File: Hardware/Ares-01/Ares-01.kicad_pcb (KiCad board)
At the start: 2 copper layers, 31 parts, among them J1 BTS7960_1, J12 XT60, J13 TCRT5000_1, J14 TCRT5000_2, J15 TCRT5000_3, J2 BTS7960_2, J3 Sharp, J4 Sharp, J5 Sharp, J6 Sharp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

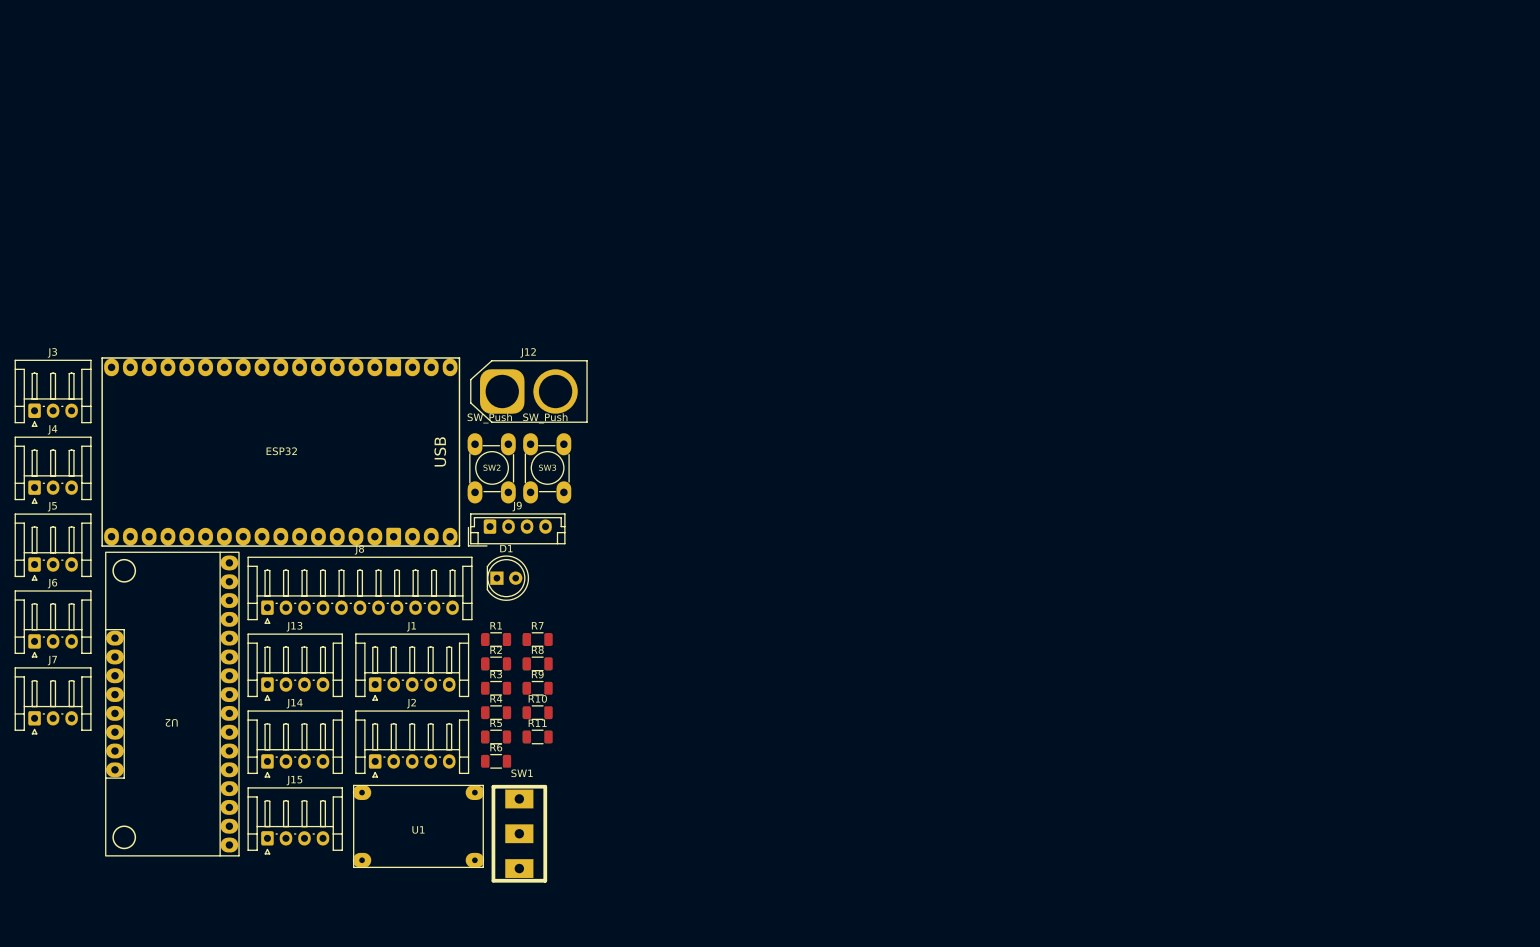
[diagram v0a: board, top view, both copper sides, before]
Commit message: Actualizacion de huellas
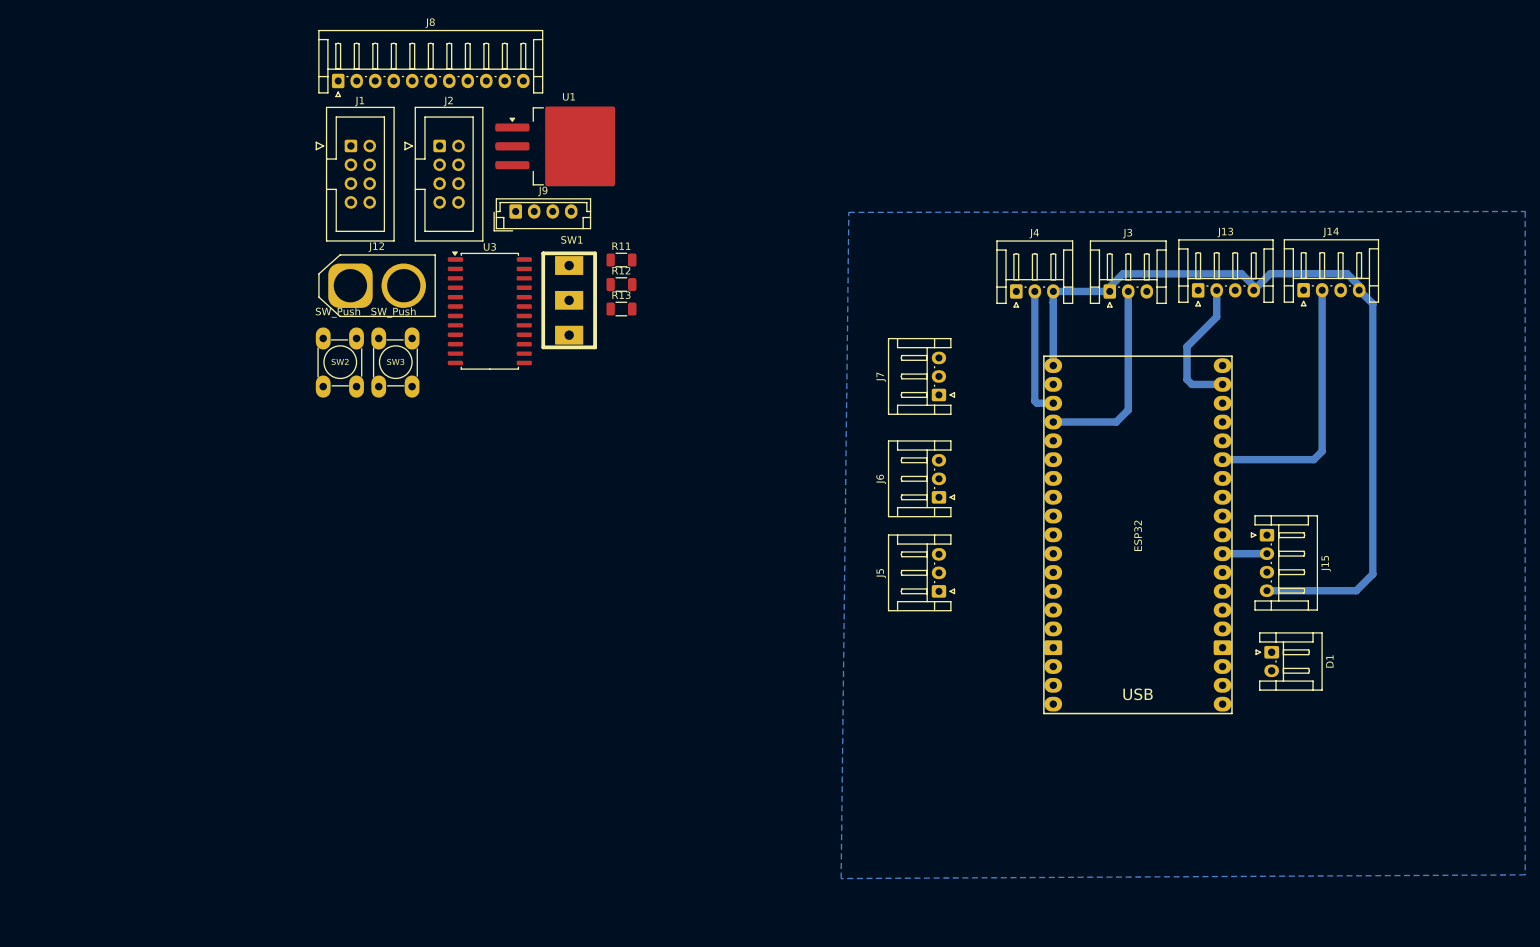
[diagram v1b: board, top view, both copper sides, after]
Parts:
- removed R1, R3, R5, R7, R9: 10k, Resistor_SMD:R_1206_3216Metric
- removed R10, R2, R4, R6, R8: 20k, Resistor_SMD:R_1206_3216Metric
- removed U2: CD74HC4067M, RamLib:CD74HC4067_module
- added R12: 220, Resistor_SMD:R_1206_3216Metric, F.Cu at (112.8, 28.4)
- added R13: 220, Resistor_SMD:R_1206_3216Metric, F.Cu at (112.8, 31.8)
- added U3: CD74HC4067M, Package_SO:SOIC-24W_7.5x15.4mm_P1.27mm, F.Cu at (95.1, 32.0)
- D1: footprint LED_THT:LED_D5.0mm -> Connector_JST:JST_EH_S2B-EH_1x02_P2.50mm_Horizontal
- ESP32: footprint RamLib:Nodemcu_ESP32S_38pin -> RamLib 2:Nodemcu_ESP32S_38pin
- J1, J2: footprint Connector_JST:JST_EH_S5B-EH_1x05_P2.50mm_Horizontal -> Connector_IDC:IDC-Header_2x04_P2.54mm_Vertical
- J9: value Conn_01x04_Pin -> Ssd1306 Arduino Pic
- SW1: footprint RamLib:SW_SPDT_TH_Vertical -> EESTN5 2:SW_SPDT_TH_Vertical
- SW2, SW3: footprint RamLib:PUSH_SWITCH_THT -> EESTN5 2:PUSH_SWITCH_THT
- U1: value Mini360 -> L7805; footprint Mini360_step-down:Mini360_step-down -> Package_TO_SOT_SMD:TO-263-3_TabPin2
- moved J14 153.7 mm to (205.0, 29.2)
- moved J3 146.1 mm to (178.8, 29.4)
- moved J15 141.1 mm to (200.0, 62.3), turned to -90 degrees
- moved J13 136.5 mm to (190.7, 29.2)
- moved J4 135.2 mm to (166.2, 29.4)
- moved J7 129.7 mm to (155.7, 43.4), turned to 90 degrees
- moved J6 123.7 mm to (155.7, 57.2), turned to 90 degrees
- moved J5 122.2 mm to (155.7, 69.9), turned to 90 degrees
- moved ESP32 116.3 mm to (182.6, 62.2), turned to -90 degrees
- moved D1 105.1 mm to (200.7, 78.1), turned to -90 degrees
- moved U1 94.1 mm to (105.8, 9.78)
- moved J2 83.6 mm to (88.3, 9.73)
- moved J1 72.8 mm to (76.3, 9.73)
- moved SW1 72.3 mm to (105.8, 30.6)
- moved J8 71.8 mm to (74.6, 0.95)
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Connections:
- D1 pad 1: LED -> Net-(D1-K)
- D1 pad 2: Net-(D1-A) -> LED
- ESP32 pad 14: unconnected-(ESP32-GND-Pad14) -> GND
- ESP32 pad 29: OUT_B -> S2
- ESP32 pad 3: OUT1 -> OUT2
- ESP32 pad 32: unconnected-(ESP32-GND-Pad32) -> GND
- ESP32 pad 33: S2 -> OUT_B
- ESP32 pad 38: unconnected-(ESP32-GND-Pad38) -> GND
- ESP32 pad 4: OUT2 -> OUT1
- ESP32 pad 6: OUT4 -> OUT5
- ESP32 pad 7: OUT5 -> OUT4
- J3 pad 1: VCC -> 3.3V
- J3 pad 2: Net-(J3-Pin_2) -> OUT1
- J4 pad 1: VCC -> GND
- J4 pad 2: Net-(J4-Pin_2) -> OUT2
- J4 pad 3: GND -> 3.3V
- J5 pad 1: VCC -> GND
- J5 pad 2: Net-(J5-Pin_2) -> OUT3
- J5 pad 3: GND -> 3.3V
- J6 pad 1: VCC -> 3.3V
- J6 pad 2: Net-(J6-Pin_2) -> OUT4
- J7 pad 1: VCC -> GND
- J7 pad 2: Net-(J7-Pin_2) -> OUT5
- J7 pad 3: GND -> 3.3V
- R11 pad 2: Net-(D1-A) -> Net-(D1-K)
- SW2 pad 2: GND -> Net-(R12-Pad2)
- SW3 pad 2: GND -> Net-(R13-Pad2)
- U1 pad 1: GND -> Net-(SW1-A)
- U1 pad 2: Net-(SW1-A) -> GND
- U1 pad 3: GND -> VCC
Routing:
- net 3.3V: track 0.00 -> 110.5 mm
- net OUT_B: track 0.00 -> 35.7 mm
- net OUT1: track 0.00 -> 26.8 mm
- net OUT_A: track 0.00 -> 18.8 mm
- net OUT2: track 0.00 -> 17.4 mm
- net OUT_C: track 0.00 -> 6.00 mm
- added copper zone on B.Cu, net GND

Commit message: primer version del pcb
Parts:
- added C2: 0,1 µF, Capacitor_SMD:C_1206_3216Metric_Pad1.33x1.80mm_HandSolder, B.Cu at (204.3, 103.8)
- added C3: 0,1uf, Capacitor_SMD:C_1206_3216Metric_Pad1.33x1.80mm_HandSolder, B.Cu at (205.0, 110.4)
- D1: footprint Connector_JST:JST_EH_S2B-EH_1x02_P2.50mm_Horizontal -> Connector_JST:JST_EH_B2B-EH-A_1x02_P2.50mm_Vertical
- J1: value BTS7960_1 -> BTS7960
- J13, J14, J15: footprint Connector_JST:JST_EH_S4B-EH_1x04_P2.50mm_Horizontal -> Connector_JST:JST_EH_B4B-EH-A_1x04_P2.50mm_Vertical
- J2: value BTS7960_2 -> BTS7960
- J3, J4, J5, J6, J7: footprint Connector_JST:JST_EH_S3B-EH_1x03_P2.50mm_Horizontal -> Connector_JST:JST_EH_B3B-EH-A_1x03_P2.50mm_Vertical
- J8: footprint Connector_JST:JST_EH_S11B-EH_1x11_P2.50mm_Horizontal -> Connector_JST:JST_EH_B10B-EH-A_1x10_P2.50mm_Vertical
- R11, R12, R13, U1: moved to B.Cu
- SW1: footprint EESTN5 2:SW_SPDT_TH_Vertical -> EESTN5:SW_SPDT_TH_Vertical
- SW2, SW3: footprint EESTN5 2:PUSH_SWITCH_THT -> EESTN5:PUSH_SWITCH_THT
- U3: footprint Package_SO:SOIC-24W_7.5x15.4mm_P1.27mm -> RamLib:CD74HC4067_module; moved to B.Cu
- moved J8 173.8 mm to (222.9, 91.4), turned to 90 degrees
- moved J1 152.5 mm to (204.0, 93.1), turned to -90 degrees
- moved U1 148.4 mm to (218.4, 106.3)
- moved J2 125.2 mm to (181.7, 93.1), turned to -90 degrees
- moved U3 119.9 mm to (209.7, 67.3), turned to 180 degrees
- moved J12 110.8 mm to (151.9, 109.6), turned to 90 degrees
- moved SW3 89.9 mm to (160.9, 75.0)
- moved J9 89.5 mm to (186.5, 35.5), turned to 180 degrees
- moved SW2 87.7 mm to (151.0, 75.0)
- moved SW1 78.0 mm to (151.9, 93.5), turned to -90 degrees
- moved R13 75.5 mm to (165.4, 85.9), turned to 90 degrees
- moved R12 71.6 mm to (155.5, 85.9), turned to 90 degrees
- moved R11 59.6 mm to (154.6, 67.7)
- moved D1 42.3 mm to (159.7, 67.7), turned to 0 degrees
- moved J4 33.3 mm to (162.2, 62.4), turned to 180 degrees
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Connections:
- ESP32 pad 11: EN_1 -> LED
- ESP32 pad 12: RPWM_2 -> B1
- ESP32 pad 15: EN_1 -> B2
- ESP32 pad 26: LED -> RPWM_2
- ESP32 pad 27: LPWM_2 -> COM
- ESP32 pad 28: OUT_C -> S0
- ESP32 pad 29: S2 -> S1
- ESP32 pad 3: OUT2 -> LPWM_2
- ESP32 pad 30: S0 -> S2
- ESP32 pad 31: S1 -> S3
- ESP32 pad 33: OUT_B -> SCL
- ESP32 pad 36: S3 -> SDA
- ESP32 pad 37: OUT_A -> unconnected-(ESP32-G23-Pad37)
- ESP32 pad 4: OUT1 -> OUT5
- ESP32 pad 5: OUT3 -> OUT4
- ESP32 pad 6: OUT5 -> OUT3
- ESP32 pad 7: OUT4 -> OUT1
- ESP32 pad 8: COM -> OUT2
- J1 pad 1: RPWM_1 -> VCC
- J1 pad 2: LPWM_1 -> GND
- J1 pad 3: EN_1 -> unconnected-(J1-Pin_3-Pad3)
- J1 pad 4: VCC -> unconnected-(J1-Pin_4-Pad4)
- J1 pad 5: GND -> VCC
- J1 pad 6: (no net) -> VCC
- J1 pad 7: (no net) -> RPWM_2
- J1 pad 8: (no net) -> LPWM_2
- J2 pad 1: RPWM_2 -> VCC
- J2 pad 2: LPWM_2 -> GND
- J2 pad 3: EN_2 -> unconnected-(J2-Pin_3-Pad3)
- J2 pad 4: VCC -> unconnected-(J2-Pin_4-Pad4)
- J2 pad 5: GND -> VCC
- J2 pad 6: (no net) -> VCC
- J2 pad 7: (no net) -> RPWM_1
- J2 pad 8: (no net) -> LPWM_1
- J3 pad 1: 3.3V -> OUT1
- J3 pad 2: OUT1 -> GND
- J3 pad 3: GND -> 3.3V
- J4 pad 1: GND -> OUT2
- J4 pad 2: OUT2 -> GND
- J5 pad 1: GND -> OUT3
- J5 pad 2: OUT3 -> GND
- J6 pad 1: 3.3V -> OUT4
- J6 pad 2: OUT4 -> GND
- J6 pad 3: GND -> 3.3V
- J7 pad 1: GND -> OUT5
- J7 pad 2: OUT5 -> GND
- U3 pad 21: unconnected-(U3-I10-Pad21) -> OUT_C
- U3 pad 22: B2 -> OUT_A
- U3 pad 23: B1 -> OUT_B
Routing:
- net VCC: track 0.00 -> 83.9 mm
- net LPWM_2: track 0.00 -> 70.5 mm
- net Net-(SW1-A): track 0.00 -> 68.6 mm
- net LPWM_1: track 0.00 -> 39.9 mm
- net RPWM_1: track 0.00 -> 38.6 mm
- net RPWM_2: track 0.00 -> 30.1 mm
- net 3.3V: track 110.5 -> 137.8 mm
- net SCL: track 0.00 -> 26.0 mm
- net B1: track 0.00 -> 20.0 mm
- net OUT_C: track 6.00 -> 25.6 mm
- net OUT1: track 26.8 -> 10.0 mm
- net SDA: track 0.00 -> 15.6 mm
- net OUT_A: track 18.8 -> 32.6 mm
- net OUT5: track 0.00 -> 11.1 mm
- net LED: track 0.00 -> 10.2 mm
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
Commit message: primera version del pcb,2
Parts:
- added C4: 0,1uf, Capacitor_SMD:C_1206_3216Metric_Pad1.33x1.80mm_HandSolder, B.Cu at (192.4, 105.4)
- added C5: 0,1 µF, Capacitor_SMD:C_1206_3216Metric_Pad1.33x1.80mm_HandSolder, B.Cu at (178.1, 111.8)
- added U2: AMS1117, Package_TO_SOT_SMD:SOT-223-3_TabPin2, B.Cu at (185.4, 108.6)
- moved R11 73.2 mm to (221.6, 97.2), turned to 180 degrees
- moved D1 64.0 mm to (216.5, 97.2), turned to 180 degrees
- moved C2 1.84 mm to (205.2, 102.2), turned to 90 degrees
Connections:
- ESP32 pad 10: LPWM_1 -> RPWM_1
- ESP32 pad 11: LED -> LPWM_1
- ESP32 pad 24: unconnected-(ESP32-G2/ADC12-Pad24) -> LED
- ESP32 pad 3: LPWM_2 -> unconnected-(ESP32-G36/ADC0-Pad3)
- ESP32 pad 9: RPWM_1 -> LPWM_2
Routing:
- net VCC: track 83.9 -> 108.3 mm
- net LED: track 10.2 -> 31.2 mm
- net LPWM_2: track 70.5 -> 49.7 mm
- net 3.3V: track 137.8 -> 143.6 mm
- net LPWM_1: track 39.9 -> 35.4 mm
- net RPWM_1: track 38.6 -> 34.4 mm
- net Net-(D1-K): track 3.66 -> 0.00 mm
- net RPWM_2: track 30.1 -> 30.9 mm

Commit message: Version 2.1 PCB
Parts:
- J12: footprint Connector_AMASS:AMASS_XT60-F_1x02_P7.20mm_Vertical -> RamLib2:XT30 connector
- moved C4 44.8 mm to (150.2, 90.5), turned to 90 degrees
- moved U2 32.7 mm to (155.9, 94.4), turned to 0 degrees
- moved C5 32.1 mm to (150.2, 96.0), turned to -90 degrees
- moved SW1 10.6 mm to (151.9, 104.1)
- moved J12 5.25 mm to (146.9, 111.1), turned to 0 degrees
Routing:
- net 3.3V: track 143.6 -> 190.0 mm
- net GND: track 0.00 -> 35.6 mm, vias 0 -> 2
- net Net-(SW1-A): track 68.6 -> 61.7 mm
- net Net-(D1-K): track 0.00 -> 3.66 mm
- net Net-(J12-Pin_2): track 8.90 -> 6.94 mm
- net VCC: track 108.3 -> 109.0 mm

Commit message: version 2.1 PCB
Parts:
- moved J15 1.38 mm to (216.4, 43.0)
- moved J13 1.23 mm to (210.2, 43.0)
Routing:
- net VCC: track 109.0 -> 117.4 mm
- net OUT_B: track 38.7 -> 40.7 mm
- net OUT_A: track 32.6 -> 30.5 mm

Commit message: version 3 del pcb
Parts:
- removed R12, R13: 220, Resistor_SMD:R_1206_3216Metric
- C2, C3, C4, C5: footprint Capacitor_SMD:C_1206_3216Metric_Pad1.33x1.80mm_HandSolder -> Capacitor_SMD:C_0805_2012Metric
- J12: value XT60 -> XT30
- J13, J14, J15, J9: footprint Connector_JST:JST_EH_B4B-EH-A_1x04_P2.50mm_Vertical -> Connector_JST:JST_XH_B4B-XH-A_1x04_P2.50mm_Vertical
- J3, J4, J5, J6, J7: footprint Connector_JST:JST_EH_B3B-EH-A_1x03_P2.50mm_Vertical -> Connector_JST:JST_XH_B3B-XH-A_1x03_P2.50mm_Vertical
- J8: footprint Connector_JST:JST_EH_B10B-EH-A_1x10_P2.50mm_Vertical -> Connector_JST:JST_XH_B10B-XH-A_1x10_P2.50mm_Vertical
- R11: footprint Resistor_SMD:R_1206_3216Metric -> Resistor_SMD:R_0805_2012Metric
- moved C4 59.1 mm to (209.2, 93.0)
- moved U2 59.1 mm to (214.9, 96.2)
- moved C5 59.0 mm to (209.2, 97.2)
- moved R11 19.8 mm to (202.1, 100.2), turned to 90 degrees
- moved D1 14.6 mm to (202.1, 95.0), turned to 90 degrees
- moved J1 13.5 mm to (194.6, 102.8), turned to 180 degrees
- moved SW2 11.5 mm to (162.5, 74.1), turned to -90 degrees
- moved J2 11.3 mm to (176.0, 102.8), turned to 180 degrees
- moved SW3 9.16 mm to (162.5, 84.0), turned to -90 degrees
- moved J12 8.19 mm to (153.4, 106.2)
- moved SW1 8.19 mm to (158.4, 99.2)
- moved J7 5.10 mm to (162.2, 36.8)
- moved J15 3.33 mm to (219.7, 43.0)
- moved C2 3.25 mm to (205.2, 105.5)
- moved J6 3.20 mm to (162.2, 43.8)
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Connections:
- ESP32 pad 1: 3.3V -> unconnected-(ESP32-3v3-Pad1)
- SW2 pad 2: Net-(R12-Pad2) -> GND
- SW3 pad 2: Net-(R13-Pad2) -> GND
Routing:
- net B2: track 5.72 -> 19.8 mm
- net LED: track 31.2 -> 21.6 mm
- net OUT5: track 11.1 -> 18.1 mm
- net GND: track 35.6 -> 41.0 mm
- net LPWM_2: track 49.7 -> 54.6 mm
- net RPWM_1: track 34.4 -> 38.5 mm
- net OUT_C: track 25.7 -> 29.6 mm
- net OUT_B: track 40.7 -> 37.4 mm
- net Net-(R13-Pad2): track 2.99 -> 0.00 mm
- net Net-(R12-Pad2): track 2.99 -> 0.00 mm
- net Net-(SW1-A): track 61.7 -> 59.0 mm
- net B1: track 20.0 -> 17.7 mm
- net OUT2: track 11.1 -> 13.4 mm
- net OUT4: track 10.0 -> 12.3 mm
- net SDA: track 15.6 -> 17.9 mm
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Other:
- board outline added: 81.5 x 87.2 mm

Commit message: Se subio las cosas faltantes
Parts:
- C2, C5: value 0,1 µF -> 100nF
- C3, C4: value 0,1uf -> 100nF
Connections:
- ESP32 pad 27: COM -> unconnected-(ESP32-G16/RX2-Pad27)
- ESP32 pad 3: unconnected-(ESP32-G36/ADC0-Pad3) -> COM
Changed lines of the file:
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@@
 	(net 14 "unconnected-(ESP32-G15{slash}ADC13-Pad23)")
 	(net 15 "unconnected-(ESP32-G6-Pad20)")
-	(net 16 "unconnected-(ESP32-G36{slash}ADC0-Pad3)")
+	(net 16 "unconnected-(ESP32-G16{slash}RX2-Pad27)")
 	(net 17 "OUT5")
 	(net 18 "unconnected-(ESP32-G10{slash}TX1-Pad17)")
@@
 			(layers "*.Cu" "*.Mask" "F.SilkS")
 			(remove_unused_layers no)
-			(net 16 "unconnected-(ESP32-G36{slash}ADC0-Pad3)")
+			(net 30 "COM")
 			(pinfunction "G36/ADC0")
 			(pintype "bidirectional")
@@
 			(layers "*.Cu" "*.Mask" "F.SilkS")
 			(remove_unused_layers no)
-			(net 30 "COM")
+			(net 16 "unconnected-(ESP32-G16{slash}RX2-Pad27)")
 			(pinfunction "G16/RX2")
 			(pintype "bidirectional")
@@
 			)
 		)
-		(property "Value" "0,1uf"
+		(property "Value" "100nF"
 			(at 0 -1.68 90)
 			(layer "B.Fab")
@@
 			)
 		)
-		(property "Value" "0,1uf"
+		(property "Value" "100nF"
 			(at 0 -1.68 270)
 			(layer "B.Fab")
@@
 			)
 		)
-		(property "Value" "0,1 µF"
+		(property "Value" "100nF"
 			(at 0 -1.68 90)
 			(layer "B.Fab")
@@
 			)
 		)
-		(property "Value" "0,1 µF"
+		(property "Value" "100nF"
 			(at 0 -1.68 270)
 			(layer "B.Fab")
